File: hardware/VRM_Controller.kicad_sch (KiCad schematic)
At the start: 0 parts

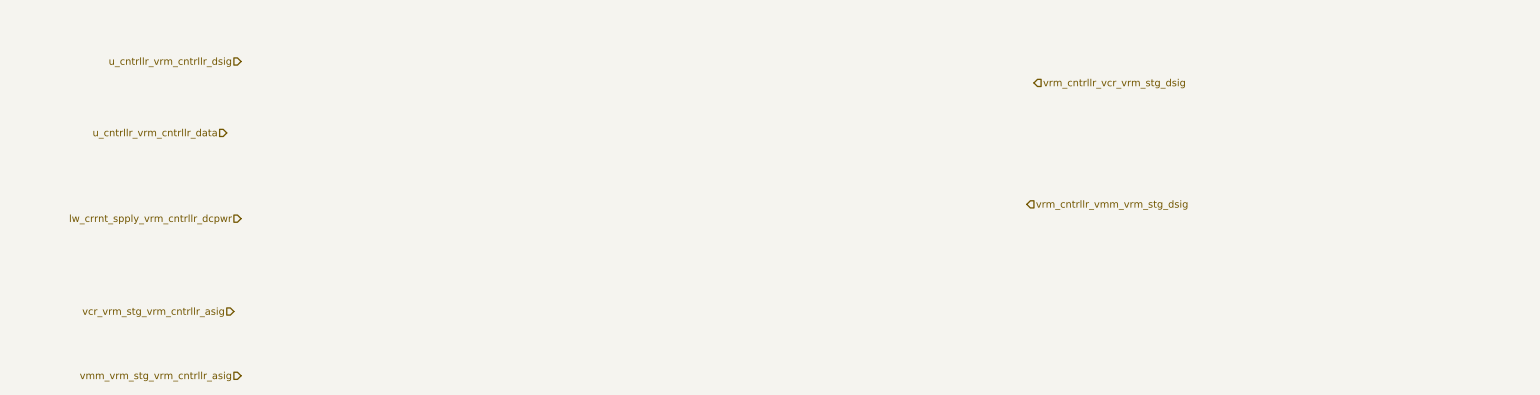
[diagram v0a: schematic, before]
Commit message: feat: added VRM IC
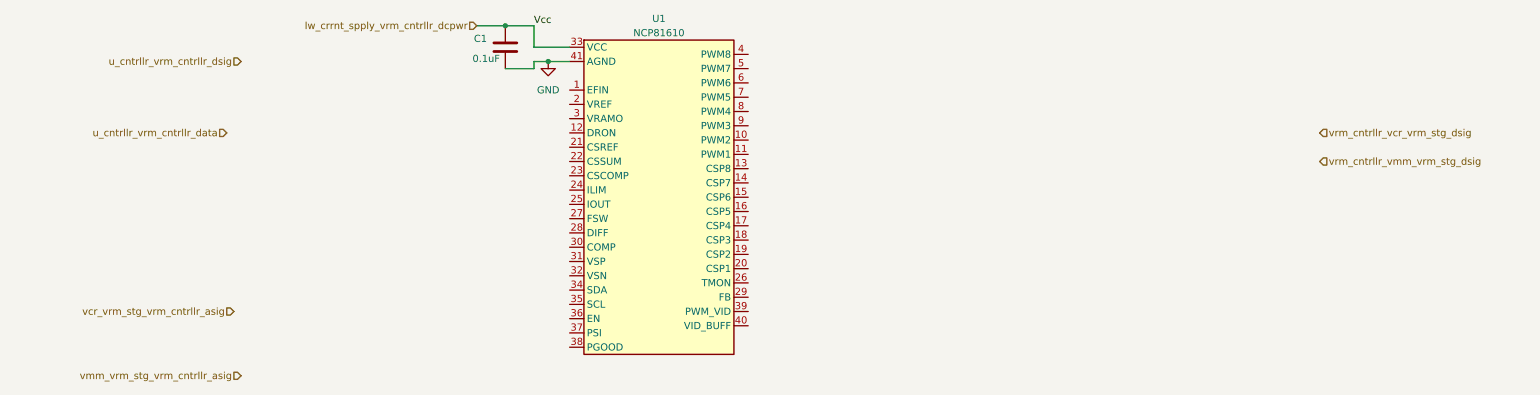
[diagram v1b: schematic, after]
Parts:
- added C1: 0.1uF, symbol Device:C
- added U1: NCP81610, Package_DFN_QFN:QFN-40-1EP_5x5mm_P0.4mm_EP3.6x3.6mm, symbol Symbol_Library:NCP81610
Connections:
- net lw_crrnt_spply_vrm_cntrllr_dcpwr: now also C1.1, U1.33 (VCC)
- new net GND: C1.2, U1.41 (AGND)

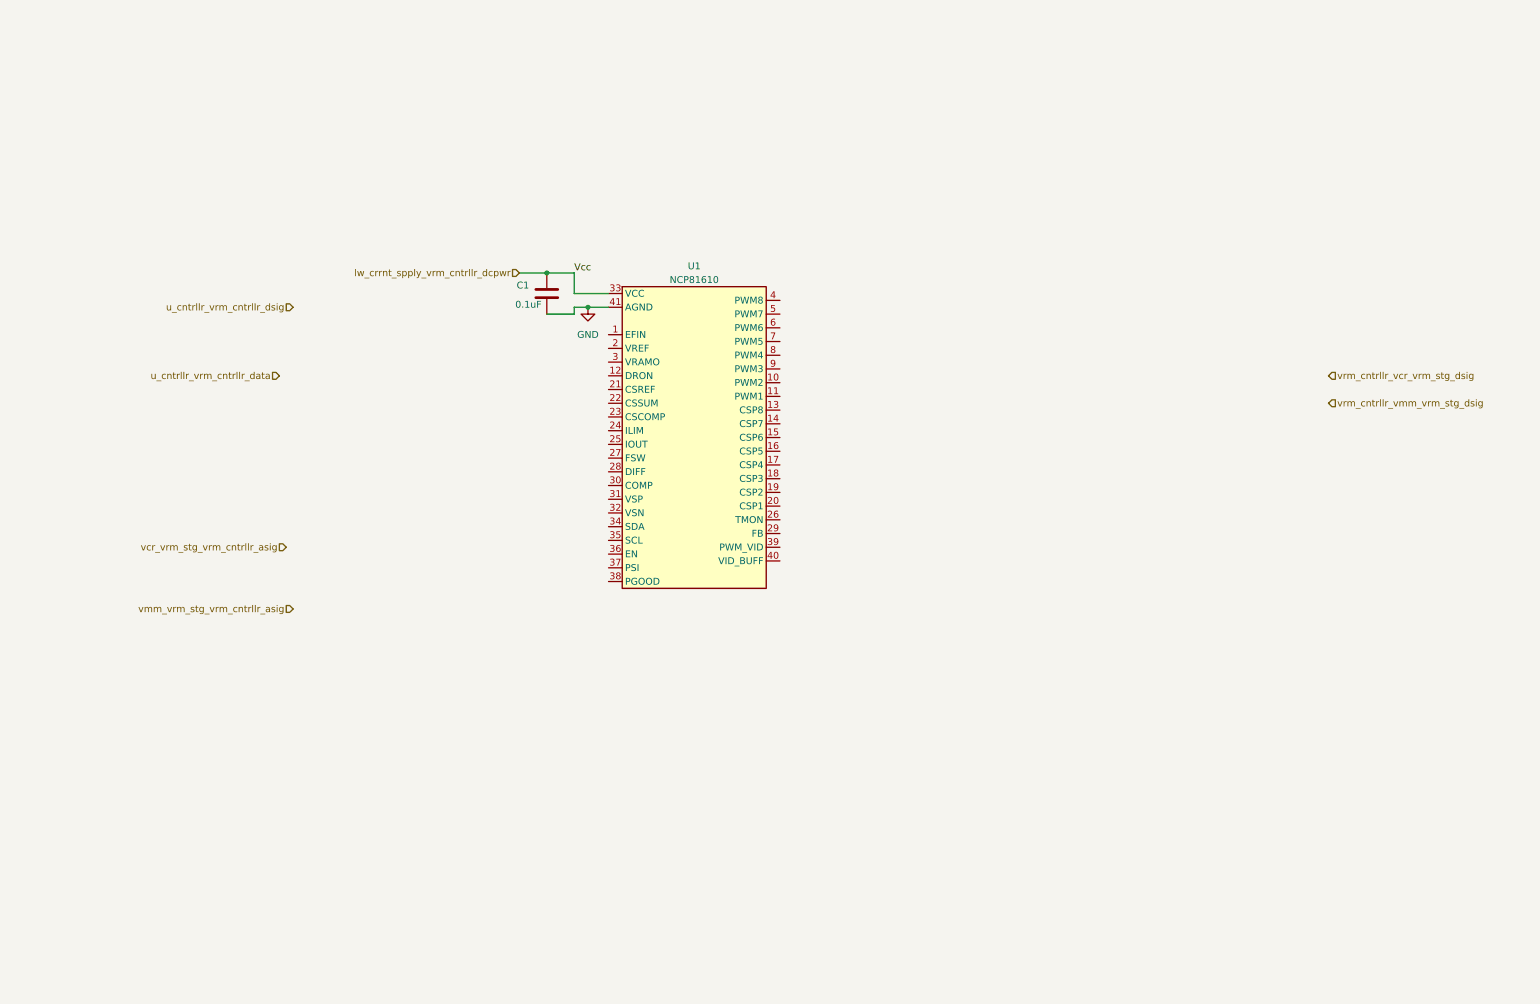
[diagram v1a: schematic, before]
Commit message: feat: new pwm controller symbol
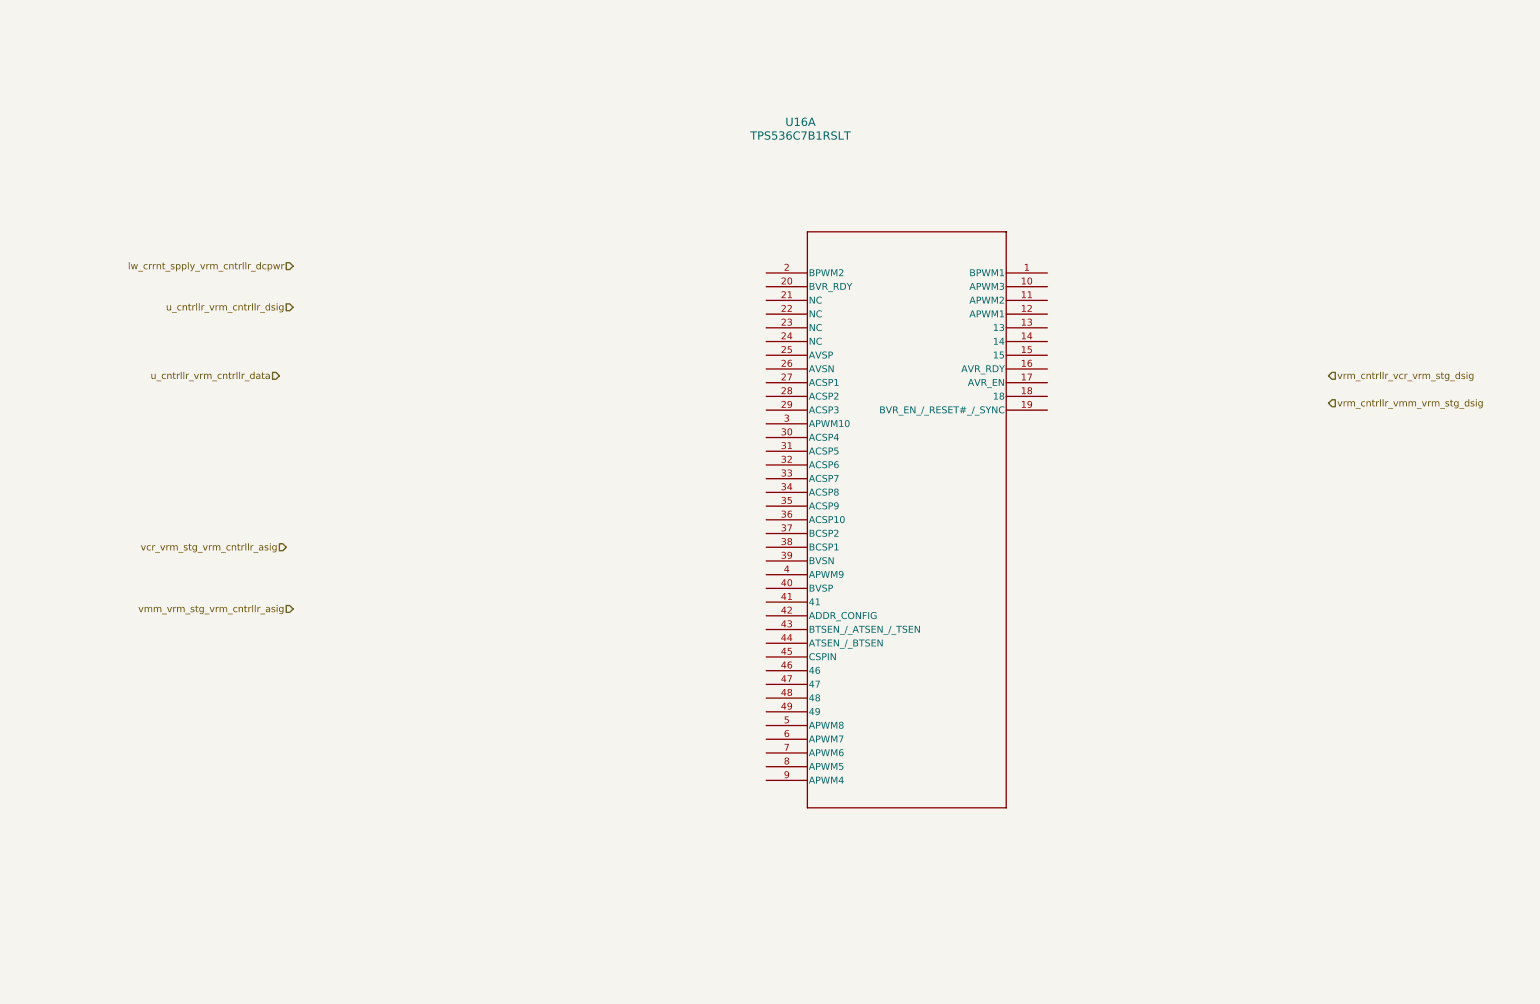
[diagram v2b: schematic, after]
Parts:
- removed C1: 0.1uF, symbol Device:C
- removed U1: NCP81610, Package_DFN_QFN:QFN-40-1EP_5x5mm_P0.4mm_EP3.6x3.6mm, symbol Symbol_Library:NCP81610
- added U16: TPS536C7B1RSLT, QFN48_6X6_TEX, symbol TPS536C7B1:TPS536C7B1RSLT

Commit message: chore: update project references
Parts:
- renumbered U16 to U2001
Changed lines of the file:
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@@
 		(dnp no)
 		(fields_autoplaced yes)
-		(property "Reference" "U16"
+		(property "Reference" "U2001"
 			(at 152.4 33.02 0)
 			(effects
@@
 			(project ""
 				(path "/d5303413-7068-41ba-88e3-39dfa38d31b7/e6dc7bfe-1f99-4466-9581-badeb70bd091"
-					(reference "U16")
+					(reference "U2001")
 					(unit 1)
 				)

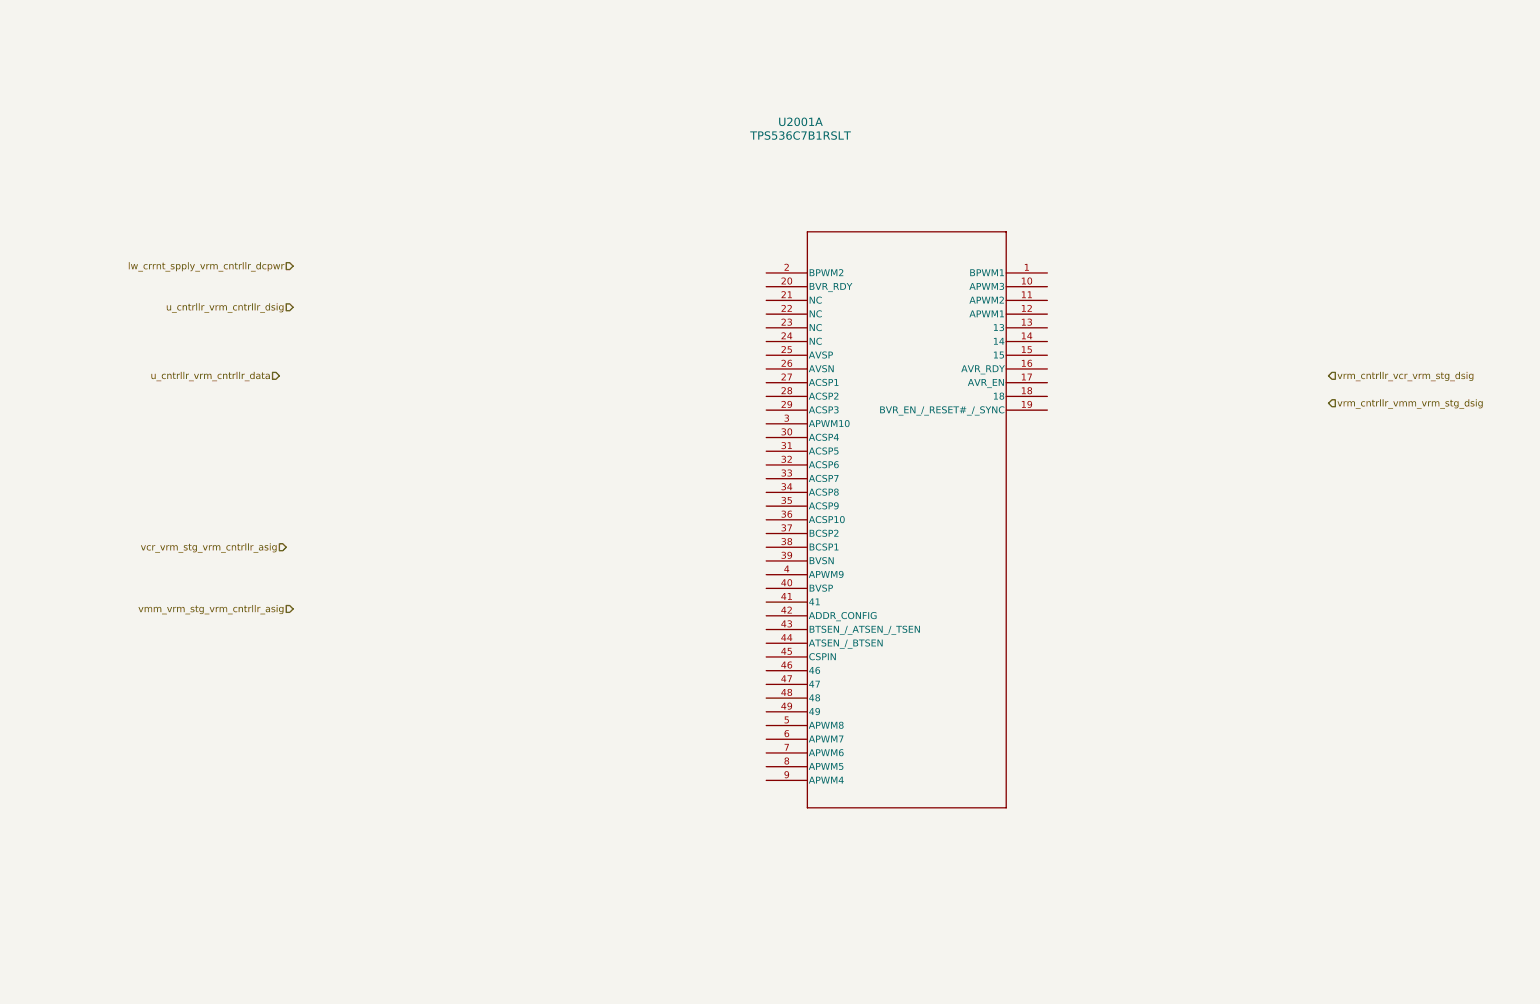
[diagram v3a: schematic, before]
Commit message: feat(schematic): set PMBUS address and channel A starting voltage
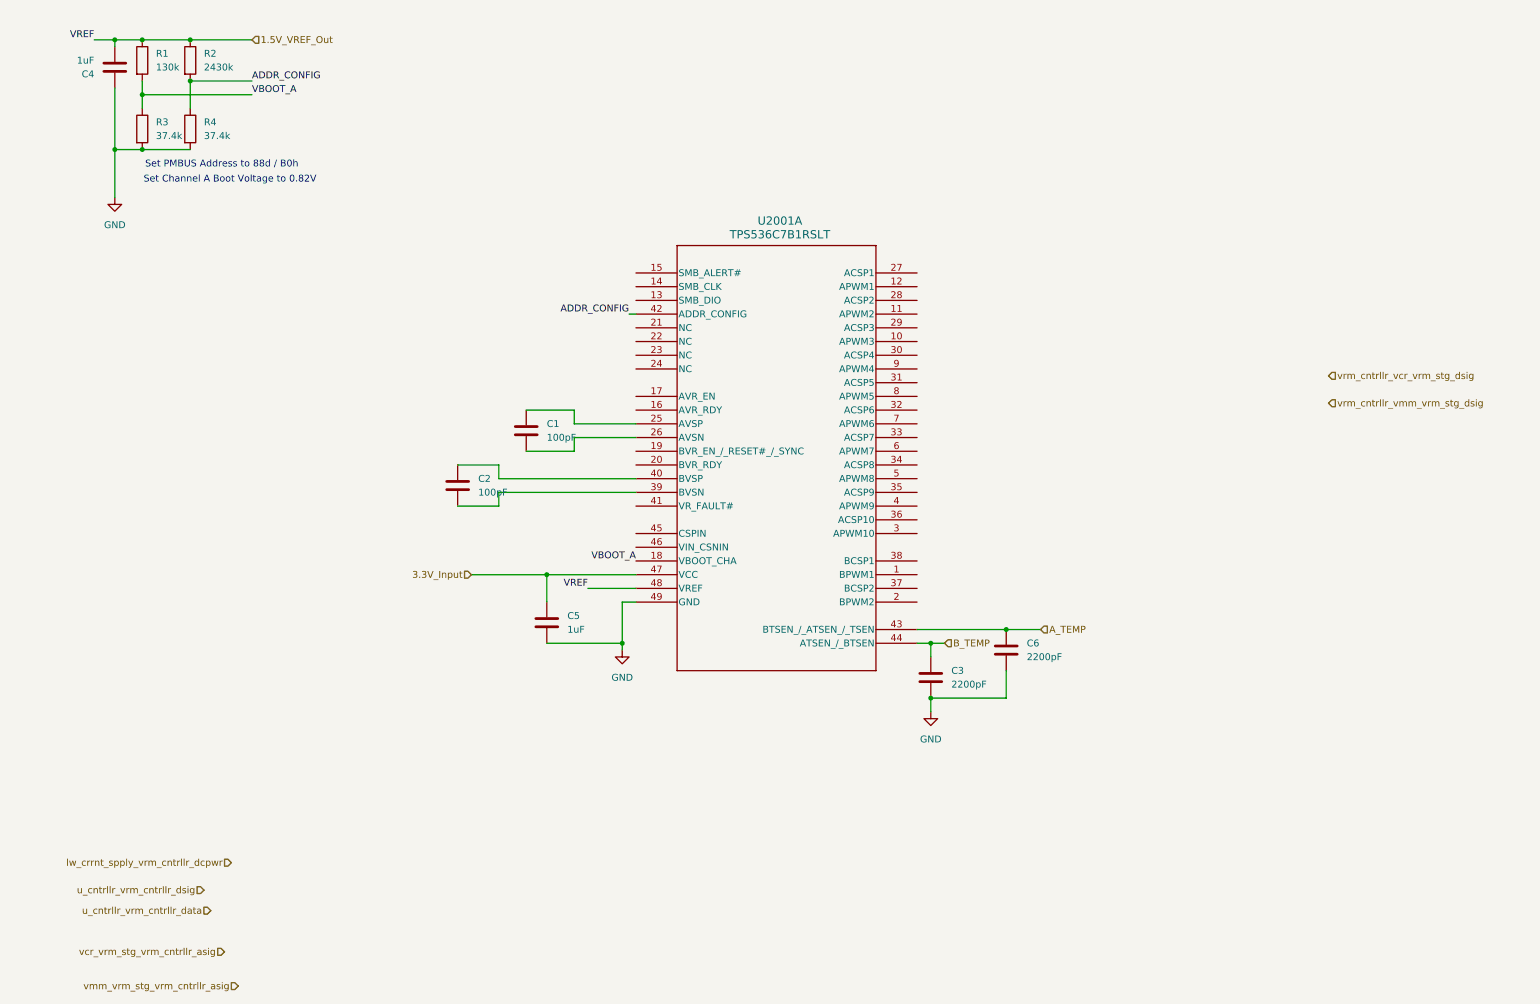
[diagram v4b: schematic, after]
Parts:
- added C1, C2: 100pF, symbol Device:C
- added C3, C6: 2200pF, symbol Device:C
- added C4, C5: 1uF, symbol Device:C
- added R1: 130k, symbol Device:R
- added R2: 2430k, symbol Device:R
- added R3, R4: 37.4k, symbol Device:R
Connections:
- net VBOOT_A: now reaches U2001.18 (VBOOT_CHA)
- net VBOOT_A: now also R1.2, R3.1
- net at U2001.25 (AVSP): now also C1.1
- net at U2001.26 (AVSN): now also C1.2
- net at U2001.39 (BVSN): now also C2.2
- net at U2001.40 (BVSP): now also C2.1
- net ADDR_CONFIG: now reaches U2001.42 (ADDR_CONFIG)
- net ADDR_CONFIG: now also R2.2, R4.1
- net A_TEMP: now reaches U2001.43 (BTSEN_/_ATSEN_/_TSEN)
- net A_TEMP: now also C6.1
- net B_TEMP: now reaches U2001.44 (ATSEN_/_BTSEN)
- net B_TEMP: now also C3.1
- net 3.3V_Input: now reaches U2001.47 (VCC)
- net 3.3V_Input: now also C5.1
- net 1.5V_VREF_Out: now reaches U2001.48 (VREF)
- net 1.5V_VREF_Out: now also C4.2, R1.1, R2.1
- net GND: now reaches U2001.49 (GND)
- net GND: now also C3.2, C4.1, C5.2, C6.2, R3.2, R4.2
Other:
- note added: "Set Channel A Boot Voltage to 0.82V"
- note added: "Set PMBUS Address to 88d / B0h"
- moved on the sheet: U2001A
